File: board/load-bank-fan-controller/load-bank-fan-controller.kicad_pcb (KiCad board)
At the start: 2 copper layers, 45.5 x 50 mm, 37 parts, among them J1 FAN1, J2 FAN2, J3 FAN3, J4 CT, J5 UART, J6 12V IN, J7 TEMP1, J8 TEMP2, J9 Conn Relay, Q1 IRF540N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

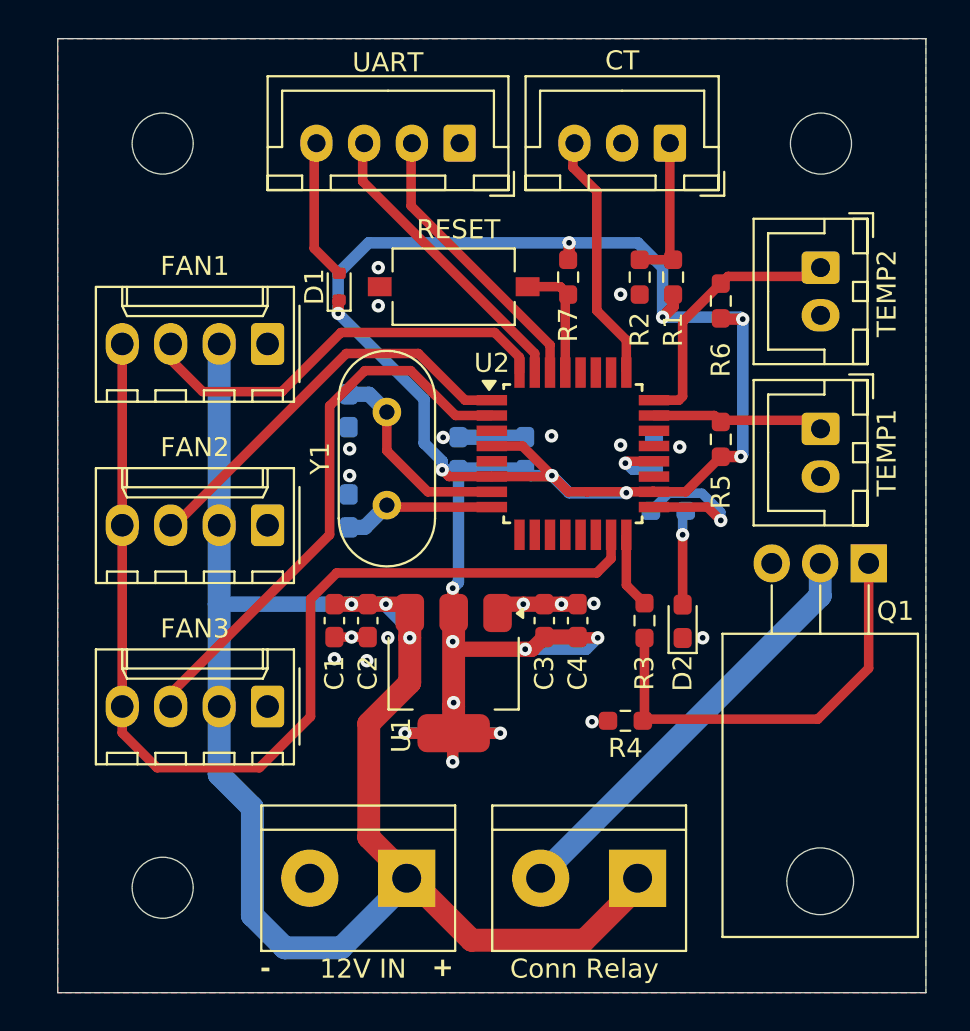
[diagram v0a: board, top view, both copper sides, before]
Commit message: change pin assignment
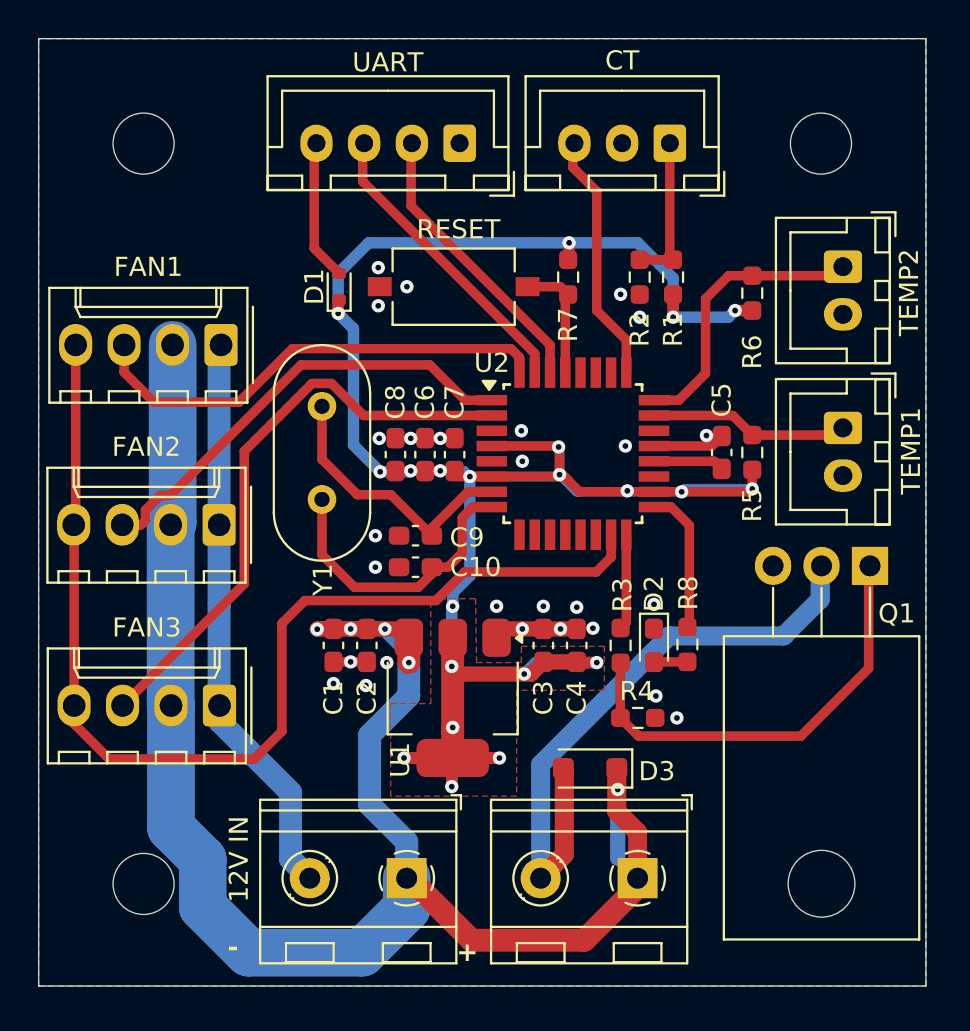
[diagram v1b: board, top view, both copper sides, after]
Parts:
- added D3: 1N4007, Diode_SMD:D_SOD-123F, F.Cu at (147.4, 118.8)
- C10, C5, C6, C7, C8, C9, R8: moved to F.Cu
- J6: footprint TerminalBlock:TerminalBlock_bornier-2_P5.08mm -> TerminalBlock_RND:TerminalBlock_RND_205-00232_1x02_P5.08mm_Horizontal
- J9: value Conn Relay -> RELAY; footprint TerminalBlock:TerminalBlock_bornier-2_P5.08mm -> TerminalBlock_RND:TerminalBlock_RND_205-00232_1x02_P5.08mm_Horizontal
- moved C9 7.43 mm to (138.2, 106.5), turned to 180 degrees
- moved R8 7.07 mm to (152.5, 112.2), turned to -90 degrees
- moved C10 4.58 mm to (138.2, 108.2), turned to 180 degrees
- moved C7 3.70 mm to (140.3, 102.3)
- moved C5 3.55 mm to (154.3, 102.2)
- moved C6 3.50 mm to (138.8, 102.3)
- moved Y1 3.41 mm to (133.3, 104.7)
- moved C8 3.30 mm to (137.2, 102.3)
- moved J2 2.54 mm to (128.0, 106.0)
- moved J3 2.52 mm to (128.0, 115.5)
- moved J1 2.44 mm to (128.1, 96.5)
- moved D2 1.96 mm to (150.8, 112.3), turned to -90 degrees
- moved R3 1.80 mm to (149.0, 112.3)
- moved R5 1.79 mm to (155.9, 102.2)
- moved R6 1.70 mm to (155.9, 93.8)
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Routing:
- net GND: track 9.89 -> 39.2 mm, vias 18 -> 27
- net Net-(D3-A): track 22.6 -> 32.3 mm
- net Net-(U2-XTAL2/PB7): track 8.02 -> 15.5 mm
- net +12V: track 86.8 -> 92.8 mm, vias 3 -> 5
- net +5V: track 134.3 -> 139.7 mm, vias 16 -> 21
- net Net-(U2-XTAL1/PB6): track 10.8 -> 14.5 mm
- net Net-(D2-A): track 4.98 -> 1.74 mm, vias 1 -> 0
- net FAN1_FB: track 22.4 -> 24.9 mm
- net FAN2_FB: track 21.6 -> 23.9 mm
- net FAN3_FB: track 29.4 -> 31.1 mm
- net FAN_PWM: track 56.2 -> 57.5 mm
- net Net-(U2-PB5): track 8.68 -> 7.53 mm, vias 1 -> 0
- net RELAY: track 3.98 -> 5.01 mm
- net TEMP1: track 9.09 -> 9.95 mm
- net Net-(Q1-G): track 22.7 -> 23.3 mm
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- added copper zone on F.Cu, net +5V
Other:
- board size 45.5 x 50 mm -> 46.5 x 49.7 mm
- board text added: "Fan Controller RD 0.0.1"
